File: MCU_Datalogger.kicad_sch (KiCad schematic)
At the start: 25 parts, among them U1 24LC1025, U2 DS1337S_, U3 24LC1025, U4 ATMEGA328P-AU, Y1 32.768 KHz, Y2 16 MHz

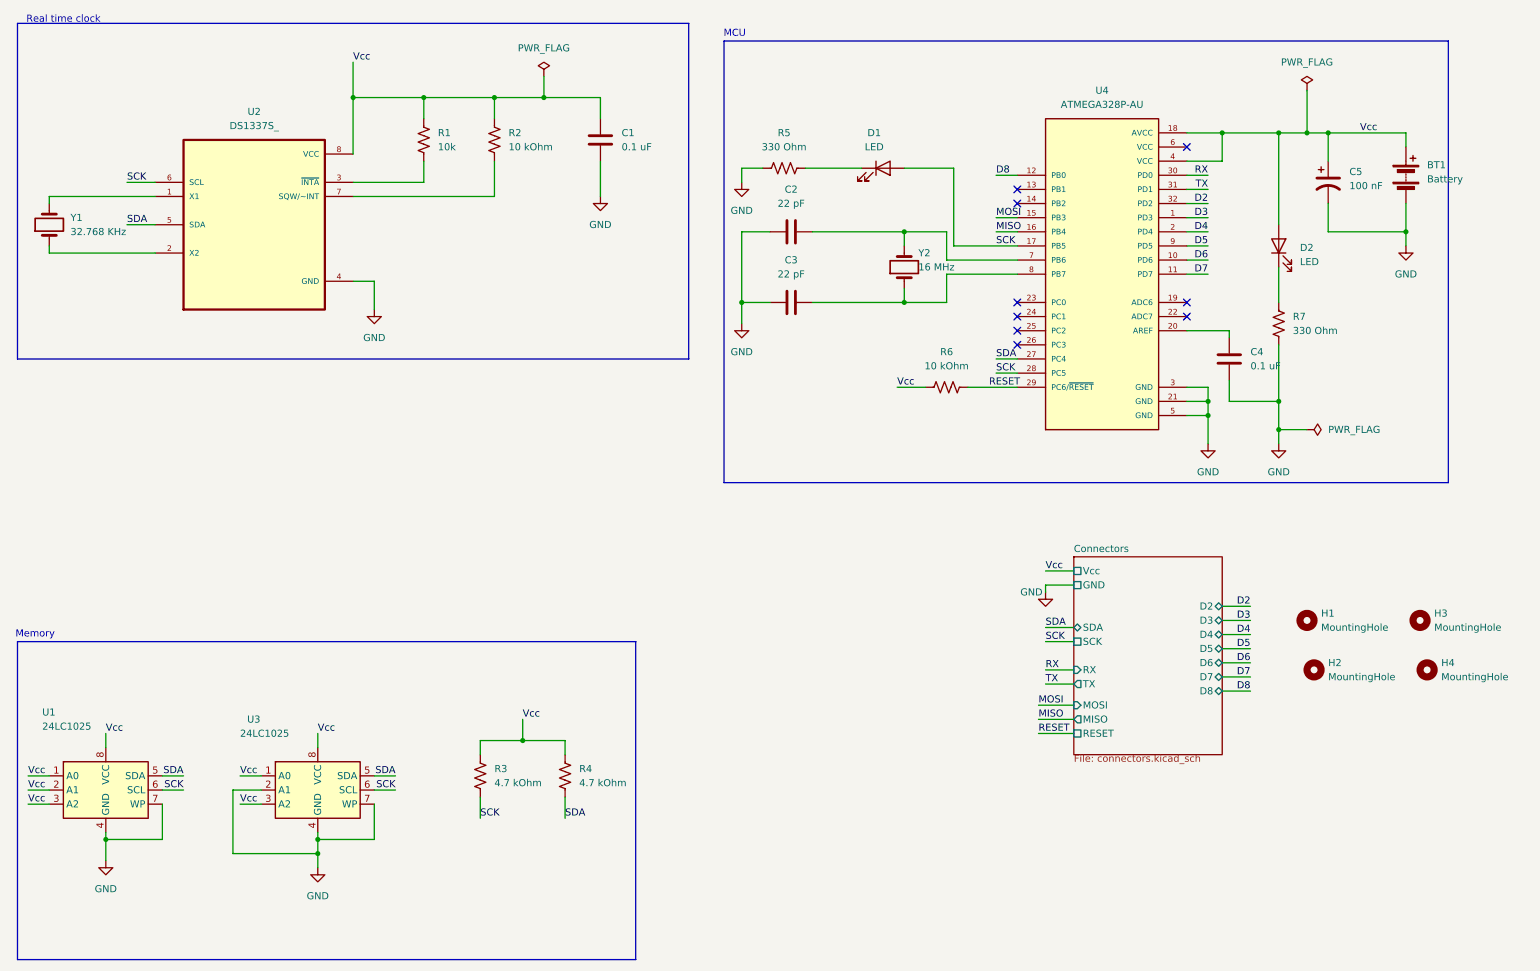
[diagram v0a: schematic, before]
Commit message: fixed bug that affects the clock
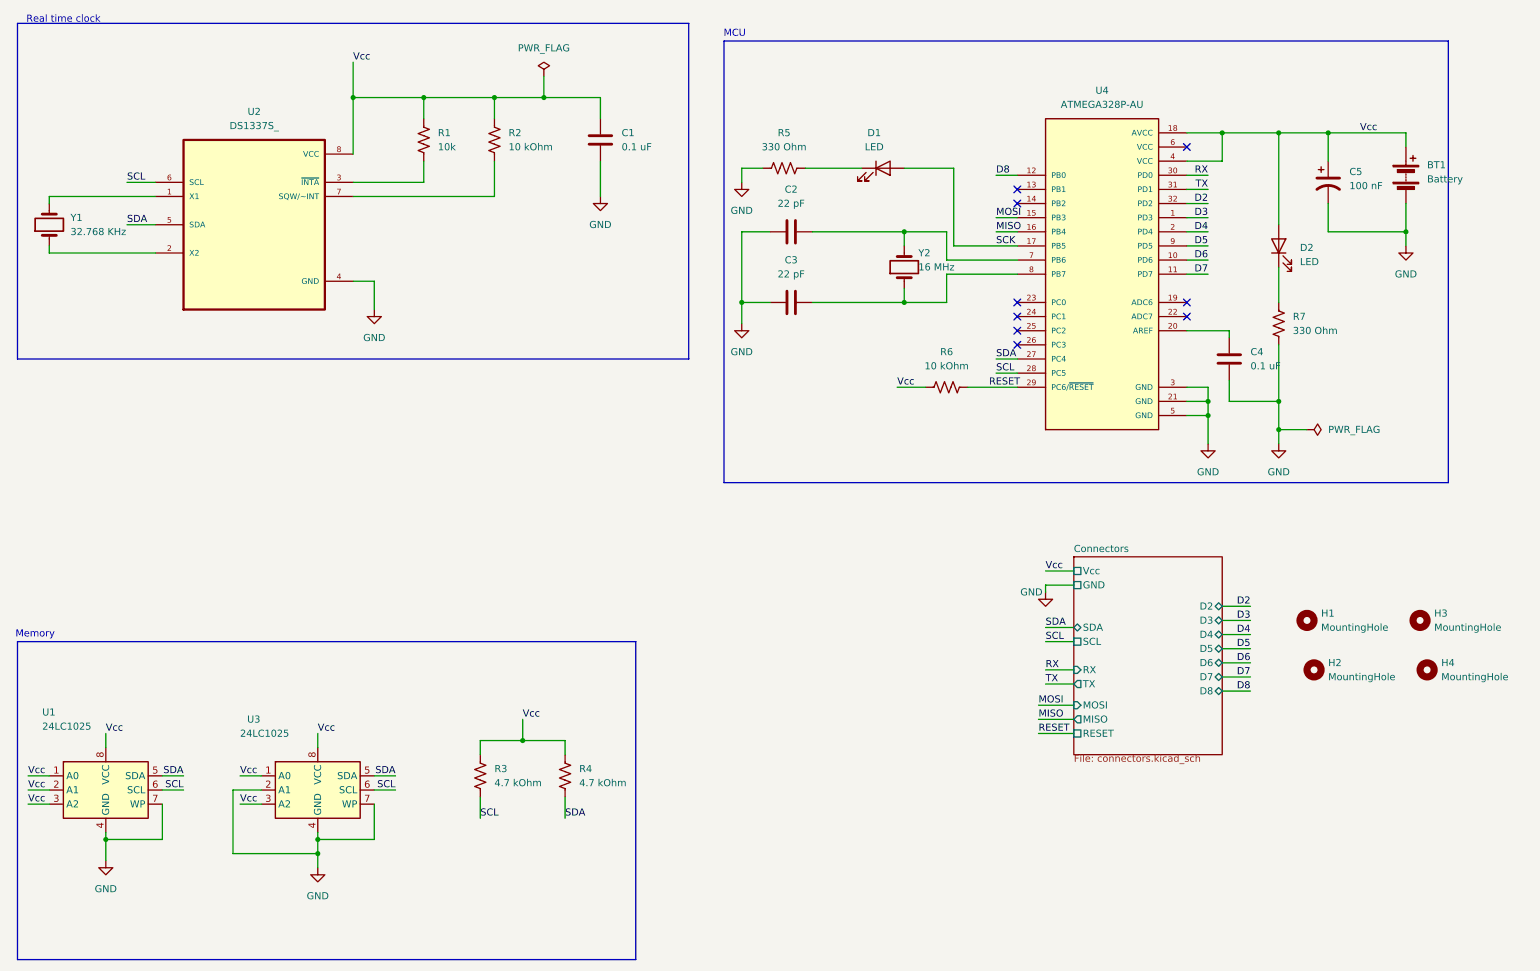
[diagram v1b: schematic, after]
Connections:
- net SCK: no longer R3.2, U1.6 (SCL), U2.6 (SCL), U3.6 (SCL), U4.28 (PC5)
- new net SCL: R3.2, U1.6 (SCL), U2.6 (SCL), U3.6 (SCL), U4.28 (PC5)
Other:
- sheet Connectors ports: added SCL; removed SCK
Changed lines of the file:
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@@
 	)
 	(junction
-		(at 110.49 29.21)
-		(diameter 0)
-		(color 0 0 0 0)
-	)
-	(junction
 		(at 265.43 53.34)
 		(diameter 0)
@@
 	)
 	(junction
+		(at 110.49 29.21)
+		(diameter 0)
+		(color 0 0 0 0)
+	)
+	(junction
 		(at 175.26 53.34)
 		(diameter 0)
@@
 		(color 0 0 0 0)
 	)
-	(junction
-		(at 247.65 35.56)
-		(diameter 0)
-		(color 0 0 0 0)
-	)
 	(no_connect
 		(at 195.58 48.26)
@@
 	(wire
 		(pts
-			(xy 110.49 29.21) (xy 120.65 29.21)
+			(xy 101.6 29.21) (xy 110.49 29.21)
 		)
 		(stroke
@@
 	(wire
 		(pts
-			(xy 251.46 35.56) (xy 247.65 35.56)
-		)
-		(stroke
-			(width 0)
-			(type default)
-		)
-	)
-	(wire
-		(pts
 			(xy 120.65 40.64) (xy 120.65 46.99)
 		)
@@
 	(wire
 		(pts
-			(xy 101.6 29.21) (xy 110.49 29.21)
-		)
-		(stroke
-			(width 0)
-			(type default)
-		)
-	)
-	(wire
-		(pts
 			(xy 232.41 35.56) (xy 226.06 35.56)
 		)
@@
 	(wire
 		(pts
-			(xy 247.65 35.56) (xy 242.57 35.56)
+			(xy 242.57 35.56) (xy 251.46 35.56)
 		)
 		(stroke
@@
 	(wire
 		(pts
-			(xy 226.06 83.82) (xy 229.87 83.82)
+			(xy 110.49 25.4) (xy 110.49 29.21)
 		)
 		(stroke
@@
 	(wire
 		(pts
-			(xy 229.87 43.18) (xy 226.06 43.18)
+			(xy 226.06 83.82) (xy 229.87 83.82)
 		)
 		(stroke
@@
 	(wire
 		(pts
-			(xy 76.2 29.21) (xy 88.9 29.21)
+			(xy 229.87 43.18) (xy 226.06 43.18)
 		)
 		(stroke
@@
 	(wire
 		(pts
-			(xy 233.68 71.12) (xy 233.68 72.39)
+			(xy 76.2 29.21) (xy 88.9 29.21)
 		)
 		(stroke
@@
 	(wire
 		(pts
-			(xy 110.49 25.4) (xy 110.49 29.21)
+			(xy 233.68 71.12) (xy 233.68 72.39)
 		)
 		(stroke
@@
 	(wire
 		(pts
-			(xy 247.65 27.94) (xy 247.65 35.56)
-		)
-		(stroke
-			(width 0)
-			(type default)
-		)
-	)
-	(wire
-		(pts
 			(xy 195.58 55.88) (xy 184.15 55.88)
 		)
@@
 	(wire
 		(pts
+			(xy 110.49 29.21) (xy 120.65 29.21)
+		)
+		(stroke
+			(width 0)
+			(type default)
+		)
+	)
+	(wire
+		(pts
 			(xy 199.39 138.43) (xy 205.74 138.43)
 		)
@@
 		)
 	)
-	(label "SCK"
+	(label "SCL"
 		(at 35.56 44.45 0)
 		(effects
@@
 		)
 	)
-	(label "SCK"
+	(label "SCL"
 		(at 191.77 78.74 0)
 		(effects
@@
 		)
 	)
-	(label "SCK"
+	(label "SCL"
 		(at 83.82 153.67 180)
 		(effects
@@
 		)
 	)
-	(label "SCK"
+	(label "SCL"
 		(at 99.06 158.75 0)
 		(effects
@@
 		)
 	)
-	(label "SCK"
+	(label "SCL"
 		(at 200.66 127 0)
 		(effects
@@
 		)
 	)
-	(label "SCK"
+	(label "SCL"
 		(at 45.72 153.67 180)
 		(effects
@@
 	)
 	(symbol
-		(lib_id "power:PWR_FLAG")
-		(at 247.65 27.94 0)
-		(unit 1)
-		(exclude_from_sim no)
-		(in_bom yes)
-		(on_board yes)
-		(dnp no)
-		(fields_autoplaced yes)
-		(property "Reference" "#FLG01"
-			(at 247.65 26.035 0)
-			(effects
-				(font
-					(size 1.27 1.27)
-				)
-				(hide yes)
-			)
-		)
-		(property "Value" "PWR_FLAG"
-			(at 247.65 22.86 0)
-			(effects
-				(font
-					(size 1.27 1.27)
-				)
-			)
-		)
-		(property "Footprint" ""
-			(at 247.65 27.94 0)
-			(effects
-				(font
-					(size 1.27 1.27)
-				)
-				(hide yes)
-			)
-		)
-		(property "Datasheet" "~"
-			(at 247.65 27.94 0)
-			(effects
-				(font
-					(size 1.27 1.27)
-				)
-				(hide yes)
-			)
-		)
-		(property "Description" "Special symbol for telling ERC where power comes from"
-			(at 247.65 27.94 0)
-			(effects
-				(font
-					(size 1.27 1.27)
-				)
-				(hide yes)
-			)
-		)
-		(pin "1"
-		)
-		(instances
-			(project ""
-				(path "/efe97554-783f-4c0b-9d08-c6cc5fac7dc5"
-					(reference "#FLG01")
-					(unit 1)
-				)
-			)
-		)
-	)
-	(symbol
 		(lib_id "power:GND")
 		(at 69.85 167.64 0)
@@
 			)
 		)
-		(pin "SCK" passive
+		(pin "SCL" passive
 			(at 205.74 127 180)
 			(effects

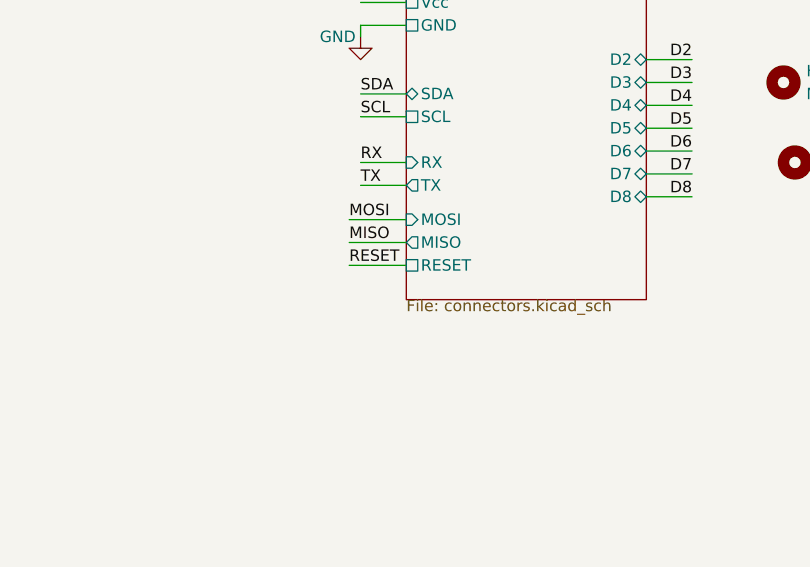
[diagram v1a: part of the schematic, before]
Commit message: fixed bug that affects the clock pt 2
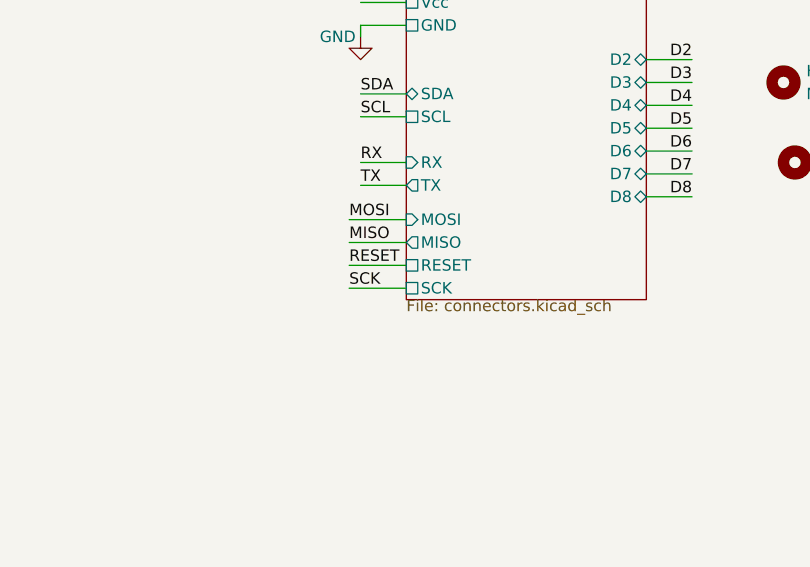
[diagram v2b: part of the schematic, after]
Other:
- sheet Connectors ports: added SCK; removed none
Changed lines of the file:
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@@
 	(wire
 		(pts
+			(xy 199.39 146.05) (xy 205.74 146.05)
+		)
+		(stroke
+			(width 0)
+			(type default)
+		)
+	)
+	(wire
+		(pts
 			(xy 229.87 45.72) (xy 226.06 45.72)
 		)
@@
 		)
 	)
+	(label "SCK"
+		(at 199.39 146.05 0)
+		(effects
+			(font
+				(size 1.27 1.27)
+			)
+			(justify left bottom)
+		)
+	)
 	(label "SDA"
 		(at 191.77 76.2 0)
@@
 			(effects
 				(font
+					(size 1.27 1.27)
+				)
+				(justify left)
+			)
+		)
+		(pin "SCK" passive
+			(at 205.74 146.05 180)
+			(effects
+				(font
